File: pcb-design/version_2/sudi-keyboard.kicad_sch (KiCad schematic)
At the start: 169 parts, among them J1 SIDE_CON, J2 SWD_JLINK, J3 0.91 OLED, J4 BatCon, J5 SIDE_CON, K1 KEYSW, K10 KEYSW, K11 KEYSW, K12 KEYSW, K13 KEYSW, K14 KEYSW, K15 KEYSW, K16 KEYSW, K17 KEYSW, K18 KEYSW, K2 KEYSW, K3 KEYSW, K4 KEYSW, K5 KEYSW, K6 KEYSW, K7 KEYSW, K8 KEYSW, K9 KEYSW, P1 USB_C_Plug_USB2.0, Q1 PJA3404_(G1,D3,S2), Q2 PJA3405_(G1,D3,S2), SW1 RST, SW3 PWR_SWITCH, SW4 5V_EN, U10 MAX17048, U4 CH340C, U5 BQ24075RGT_DPPM, U6 TPS63002_SEPIC_5V, U7 nRF52832-QFxx, U8 MCP23017_SS, U9 TPS63001_SEPIC_3V3, Y1 32MHz_CF4032M00020001

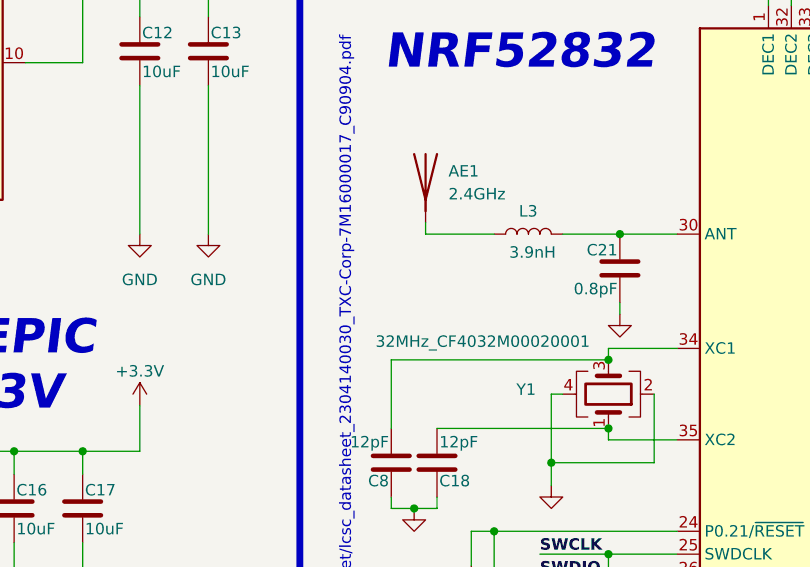
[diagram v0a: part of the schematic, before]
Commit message: [12-16-2150] add capacitor to anntena
renamed kicad project
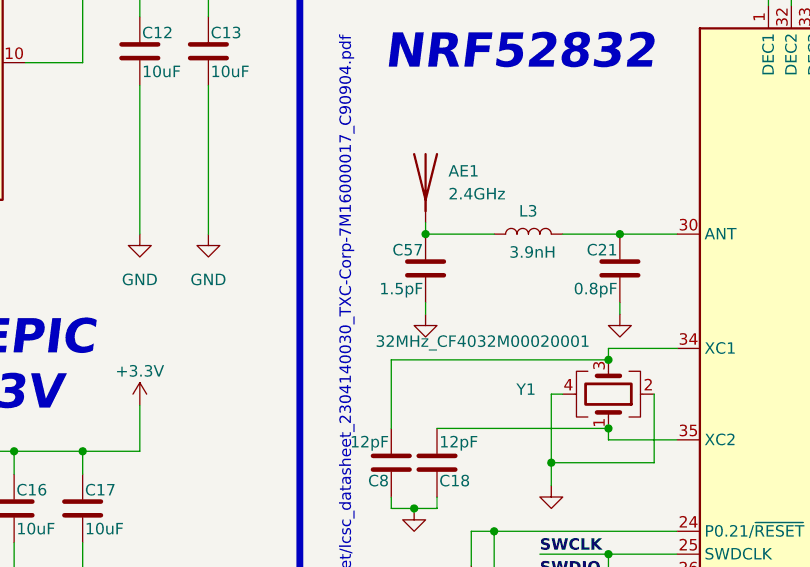
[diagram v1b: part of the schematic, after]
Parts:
- added C57: 1.5pF, Capacitor_SMD:C_0805_2012Metric_Pad1.18x1.45mm_HandSolder, symbol Device:C
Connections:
- net GND: now also C57.2
- net at AE1.1 (A), L3.1: now also C57.1
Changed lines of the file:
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@@
 	)
 	(junction
+		(at 130.81 171.45)
+		(diameter 0)
+		(color 0 0 0 0)
+	)
+	(junction
 		(at 349.25 182.88)
 		(diameter 0)
@@
 	(wire
 		(pts
+			(xy 130.81 180.34) (xy 130.81 179.07)
+		)
+		(stroke
+			(width 0)
+			(type default)
+		)
+	)
+	(wire
+		(pts
 			(xy 62.23 147.32) (xy 62.23 152.4)
 		)
@@
 	)
 	(symbol
+		(lib_id "power:GND")
+		(at 130.81 180.34 0)
+		(unit 1)
+		(exclude_from_sim no)
+		(in_bom yes)
+		(on_board yes)
+		(dnp no)
+		(fields_autoplaced yes)
+		(property "Reference" "#PWR087"
+			(at 130.81 186.69 0)
+			(effects
+				(font
+					(size 1.27 1.27)
+				)
+				(hide yes)
+			)
+		)
+		(property "Value" "GND"
+			(at 130.81 185.42 0)
+			(effects
+				(font
+					(size 1.27 1.27)
+				)
+				(hide yes)
+			)
+		)
+		(property "Footprint" ""
+			(at 130.81 180.34 0)
+			(effects
+				(font
+					(size 1.27 1.27)
+				)
+				(hide yes)
+			)
+		)
+		(property "Datasheet" ""
+			(at 130.81 180.34 0)
+			(effects
+				(font
+					(size 1.27 1.27)
+				)
+				(hide yes)
+			)
+		)
+		(property "Description" ""
+			(at 130.81 180.34 0)
+			(effects
+				(font
+					(size 1.27 1.27)
+				)
+				(hide yes)
+			)
+		)
+		(pin "1"
+		)
+		(instances
+			(project "sudi-redox-clone"
+				(path "/5bbd2338-13ff-49b0-9f87-5cbfec528c5b"
+					(reference "#PWR087")
+					(unit 1)
+				)
+			)
+		)
+	)
+	(symbol
 		(lib_id "canadian_parts:KEYSW")
 		(at 331.47 135.89 0)
@@
 					(unit 1)
 				)
+			)
+		)
+	)
+	(symbol
+		(lib_id "Device:C")
+		(at 130.81 175.26 0)
+		(mirror y)
+		(unit 1)
+		(exclude_from_sim no)
+		(in_bom yes)
+		(on_board yes)
+		(dnp no)
+		(property "Reference" "C57"
+			(at 130.556 173.228 0)
+			(effects
+				(font
+					(size 1.27 1.27)
+				)
+				(justify left)
+			)
+		)
+		(property "Value" "1.5pF"
+			(at 130.556 177.546 0)
+			(effects
+				(font
+					(size 1.27 1.27)
+				)
+				(justify left)
+			)
+		)
+		(property "Footprint" "Capacitor_SMD:C_0805_2012Metric_Pad1.18x1.45mm_HandSolder"
+			(at 129.8448 179.07 0)
+			(effects
+				(font
+					(size 1.27 1.27)
+				)
+				(hide yes)
+			)
+		)
+		(property "Datasheet" "~"
+			(at 130.81 175.26 0)
+			(effects
+				(font
+					(size 1.27 1.27)
+				)
+				(hide yes)
+			)
+		)
+		(property "Description" "Unpolarized capacitor"
+			(at 130.81 175.26 0)
+			(effects
+				(font
+					(size 1.27 1.27)
+				)
+				(hide yes)
+			)
+		)
+		(pin "1"
+		)
+		(pin "2"
+		)
+		(instances
+			(project "sudi-redox-clone"
+				(path "/5bbd2338-13ff-49b0-9f87-5cbfec528c5b"
+					(reference "C57")
+					(unit 1)
+				)

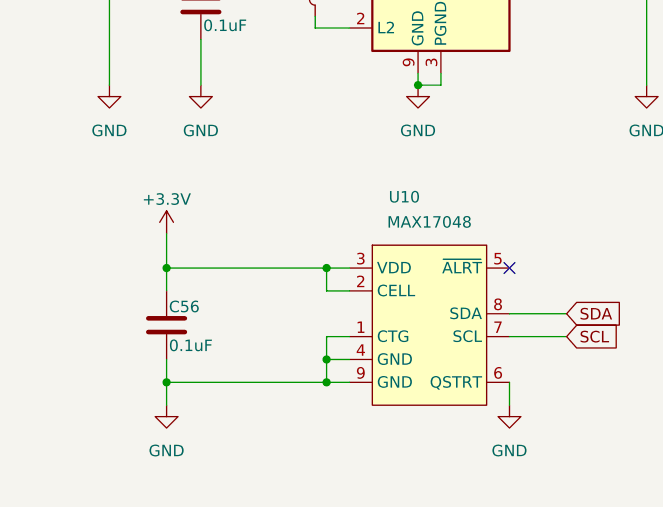
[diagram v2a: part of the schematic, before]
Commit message: feat(component): change component to correct size
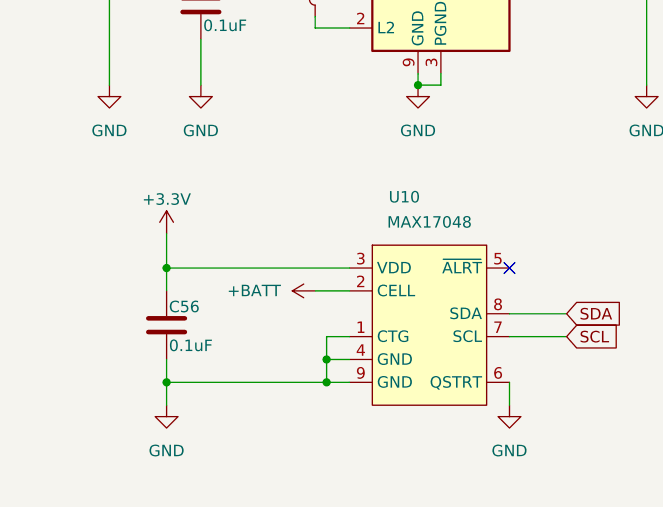
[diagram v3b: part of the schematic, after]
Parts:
- L1, L2: footprint Inductor_SMD:L_0603_1608Metric_Pad1.05x0.95mm_HandSolder -> Inductor_SMD:L_Bourns_SRP7028A_7.3x6.6mm
- Y1: footprint Crystal:Crystal_SMD_2016-4Pin_2.0x1.6mm -> Crystal:Crystal_SMD_3225-4Pin_3.2x2.5mm_HandSoldering
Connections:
- net +3.3V: no longer U10.2 (CELL)
- net +BATT: now also U10.2 (CELL)
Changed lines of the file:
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@@
 	)
 	(junction
-		(at 49.53 242.57)
-		(diameter 0)
-		(color 0 0 0 0)
-	)
-	(junction
 		(at 92.71 144.78)
 		(diameter 0)
@@
 	(wire
 		(pts
-			(xy 31.75 242.57) (xy 49.53 242.57)
-		)
-		(stroke
-			(width 0)
-			(type default)
-		)
-	)
-	(wire
-		(pts
 			(xy 309.88 180.34) (xy 318.77 180.34)
 		)
@@
 	(wire
 		(pts
-			(xy 49.53 242.57) (xy 52.07 242.57)
+			(xy 31.75 242.57) (xy 52.07 242.57)
 		)
 		(stroke
@@
 	(wire
 		(pts
+			(xy 48.26 245.11) (xy 52.07 245.11)
+		)
+		(stroke
+			(width 0)
+			(type default)
+		)
+	)
+	(wire
+		(pts
 			(xy 152.4 179.07) (xy 152.4 180.34)
 		)
@@
 	(wire
 		(pts
-			(xy 49.53 245.11) (xy 52.07 245.11)
-		)
-		(stroke
-			(width 0)
-			(type default)
-		)
-	)
-	(wire
-		(pts
 			(xy 260.35 224.79) (xy 271.78 224.79)
 		)
@@
 	(wire
 		(pts
-			(xy 49.53 242.57) (xy 49.53 245.11)
-		)
-		(stroke
-			(width 0)
-			(type default)
-		)
-	)
-	(wire
-		(pts
 			(xy 176.53 24.13) (xy 176.53 25.4)
 		)
@@
 			)
 		)
-		(property "Footprint" "Inductor_SMD:L_0603_1608Metric_Pad1.05x0.95mm_HandSolder"
+		(property "Footprint" "Inductor_SMD:L_Bourns_SRP7028A_7.3x6.6mm"
 			(at 48.26 210.82 0)
 			(effects
@@
 			)
 		)
-		(property "Footprint" "Inductor_SMD:L_0603_1608Metric_Pad1.05x0.95mm_HandSolder"
+		(property "Footprint" "Inductor_SMD:L_Bourns_SRP7028A_7.3x6.6mm"
 			(at 62.23 160.02 0)
 			(effects
@@
 			)
 		)
-		(property "Footprint" "Crystal:Crystal_SMD_2016-4Pin_2.0x1.6mm"
+		(property "Footprint" "Crystal:Crystal_SMD_3225-4Pin_3.2x2.5mm_HandSoldering"
 			(at 151.13 189.23 0)
 			(effects
@@
 					(unit 1)
 				)
+			)
+		)
+	)
+	(symbol
+		(lib_id "power:+BATT")
+		(at 48.26 245.11 90)
+		(unit 1)
+		(exclude_from_sim no)
+		(in_bom yes)
+		(on_board yes)
+		(dnp no)
+		(fields_autoplaced yes)
+		(property "Reference" "#PWR088"
+			(at 52.07 245.11 0)
+			(effects
+				(font
+					(size 1.27 1.27)
+				)
+				(hide yes)
+			)
+		)
+		(property "Value" "+BATT"
+			(at 44.45 245.1099 90)
+			(effects
+				(font
+					(size 1.27 1.27)
+				)
+				(justify left)
+			)
+		)
+		(property "Footprint" ""
+			(at 48.26 245.11 0)
+			(effects
+				(font
+					(size 1.27 1.27)
+				)
+				(hide yes)
+			)
+		)
+		(property "Datasheet" ""
+			(at 48.26 245.11 0)
+			(effects
+				(font
+					(size 1.27 1.27)
+				)
+				(hide yes)
+			)
+		)
+		(property "Description" "Power symbol creates a global label with name \"+BATT\""
+			(at 48.26 245.11 0)
+			(effects
+				(font
+					(size 1.27 1.27)
+				)
+				(hide yes)
+			)
+		)
+		(pin "1"
+		)
+		(instances
+			(project "sudi-keyboard"
+				(path "/5bbd2338-13ff-49b0-9f87-5cbfec528c5b"
+					(reference "#PWR088")
+					(unit 1)
+				)
